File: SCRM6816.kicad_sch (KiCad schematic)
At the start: 10 parts, among them U1 68HC000P16, U24 74HC08, U6 74HC32, U7 74HC14, U8 74HC05, X1 CXO_DIP8_16MHz

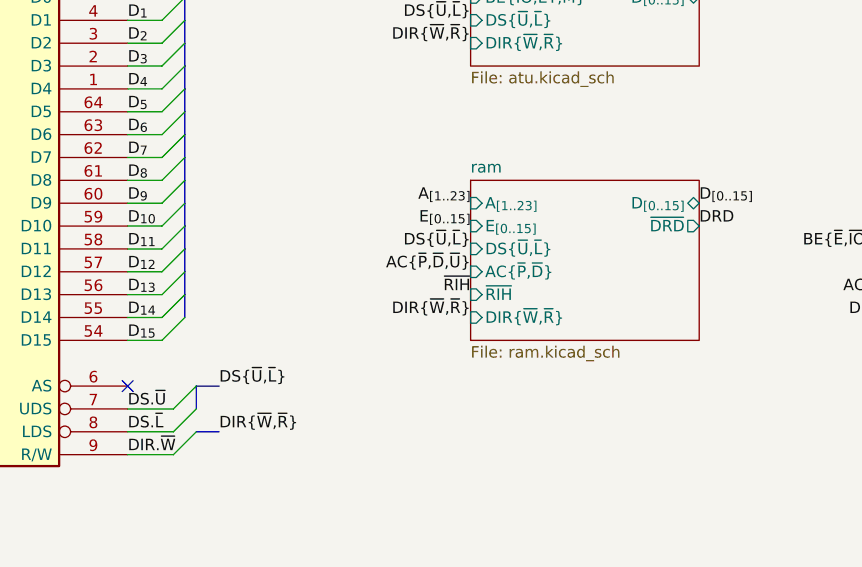
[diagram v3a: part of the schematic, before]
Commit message: apparently the ram was enabled all the time, ram.kicad_sch didn't even require BE.M... 	like whaaaaaaaa how did i let this happen oh my god sometimes im just braindead.
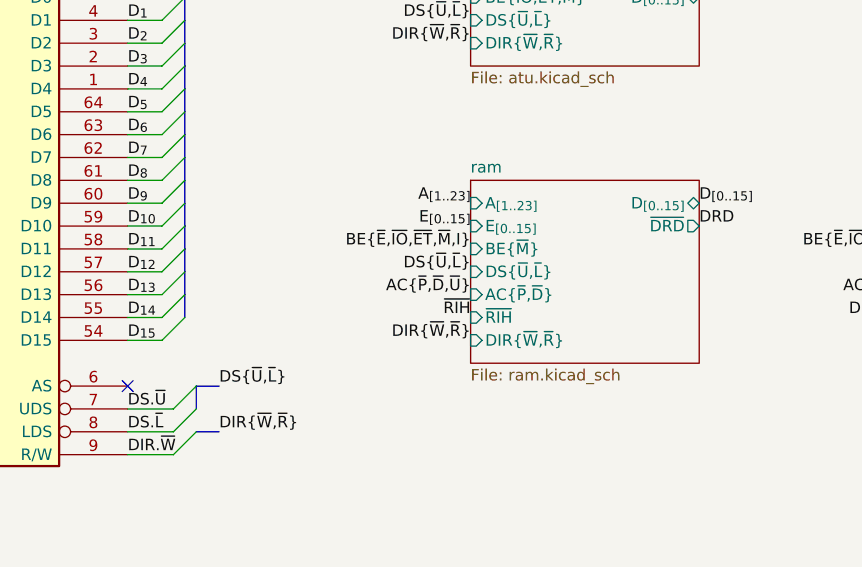
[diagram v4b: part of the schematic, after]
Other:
- sheet ram ports: added BE{~{M}}; removed none
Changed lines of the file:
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@@
 	)
 	(label "AC{~{P},~{D},~{U}}"
-		(at 127 124.46 180)
+		(at 127 127 180)
 		(effects
 			(font
@@
 	)
 	(label "DS{~{U},~{L}}"
-		(at 127 121.92 180)
+		(at 127 124.46 180)
 		(effects
 			(font
@@
 	)
 	(label "~{RIH}"
-		(at 127 127 180)
+		(at 127 129.54 180)
 		(effects
 			(font
@@
 	)
 	(label "DIR{~{W},~{R}}"
-		(at 127 129.54 180)
+		(at 127 132.08 180)
 		(effects
 			(font
@@
 		)
 	)
+	(label "BE{~{E},~{IO},~{ET},~{M},I}"
+		(at 127 121.92 180)
+		(effects
+			(font
+				(size 1.27 1.27)
+			)
+			(justify right bottom)
+		)
+	)
 	(label "~{I_{2}}"
 		(at 38.1 45.72 180)
@@
 	(sheet
 		(at 127 114.3)
-		(size 25.4 17.78)
+		(size 25.4 20.32)
 		(exclude_from_sim no)
 		(in_bom yes)
@@
 		)
 		(property "Sheetfile" "ram.kicad_sch"
-			(at 127 132.6646 0)
+			(at 127 135.2046 0)
 			(effects
 				(font
@@
 		)
 		(pin "AC{~{P},~{D}}" input
-			(at 127 124.46 180)
+			(at 127 127 180)
 			(effects
 				(font
@@
 		)
 		(pin "DIR{~{W},~{R}}" input
-			(at 127 129.54 180)
+			(at 127 132.08 180)
 			(effects
 				(font
@@
 		)
 		(pin "DS{~{U},~{L}}" input
-			(at 127 121.92 180)
+			(at 127 124.46 180)
 			(effects
 				(font
@@
 		)
 		(pin "~{RIH}" input
-			(at 127 127 180)
+			(at 127 129.54 180)
 			(effects
 				(font
@@
 			)
 		)
+		(pin "BE{~{M}}" input
+			(at 127 121.92 180)
+			(effects
+				(font
+					(size 1.27 1.27)
+				)
+				(justify left)
+			)
+		)

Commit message: [scheme] no major changes
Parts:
- added U28: 74HC74, symbol 74xx:74HC74
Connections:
- net +5V: now also U28.1 (~{R}), U28.10 (~{S}), U28.13 (~{R}), U28.4 (~{S})
- new net: U28.2 (D), U28.6 (~{Q})
- new net: U28.12 (D), U28.8 (~{Q})
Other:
- note added: "frequency dependent parts: - C1-R4 (rom's DRD timer) - C4-R12 (ilatch's timeout timer)"
- moved on the sheet: X1

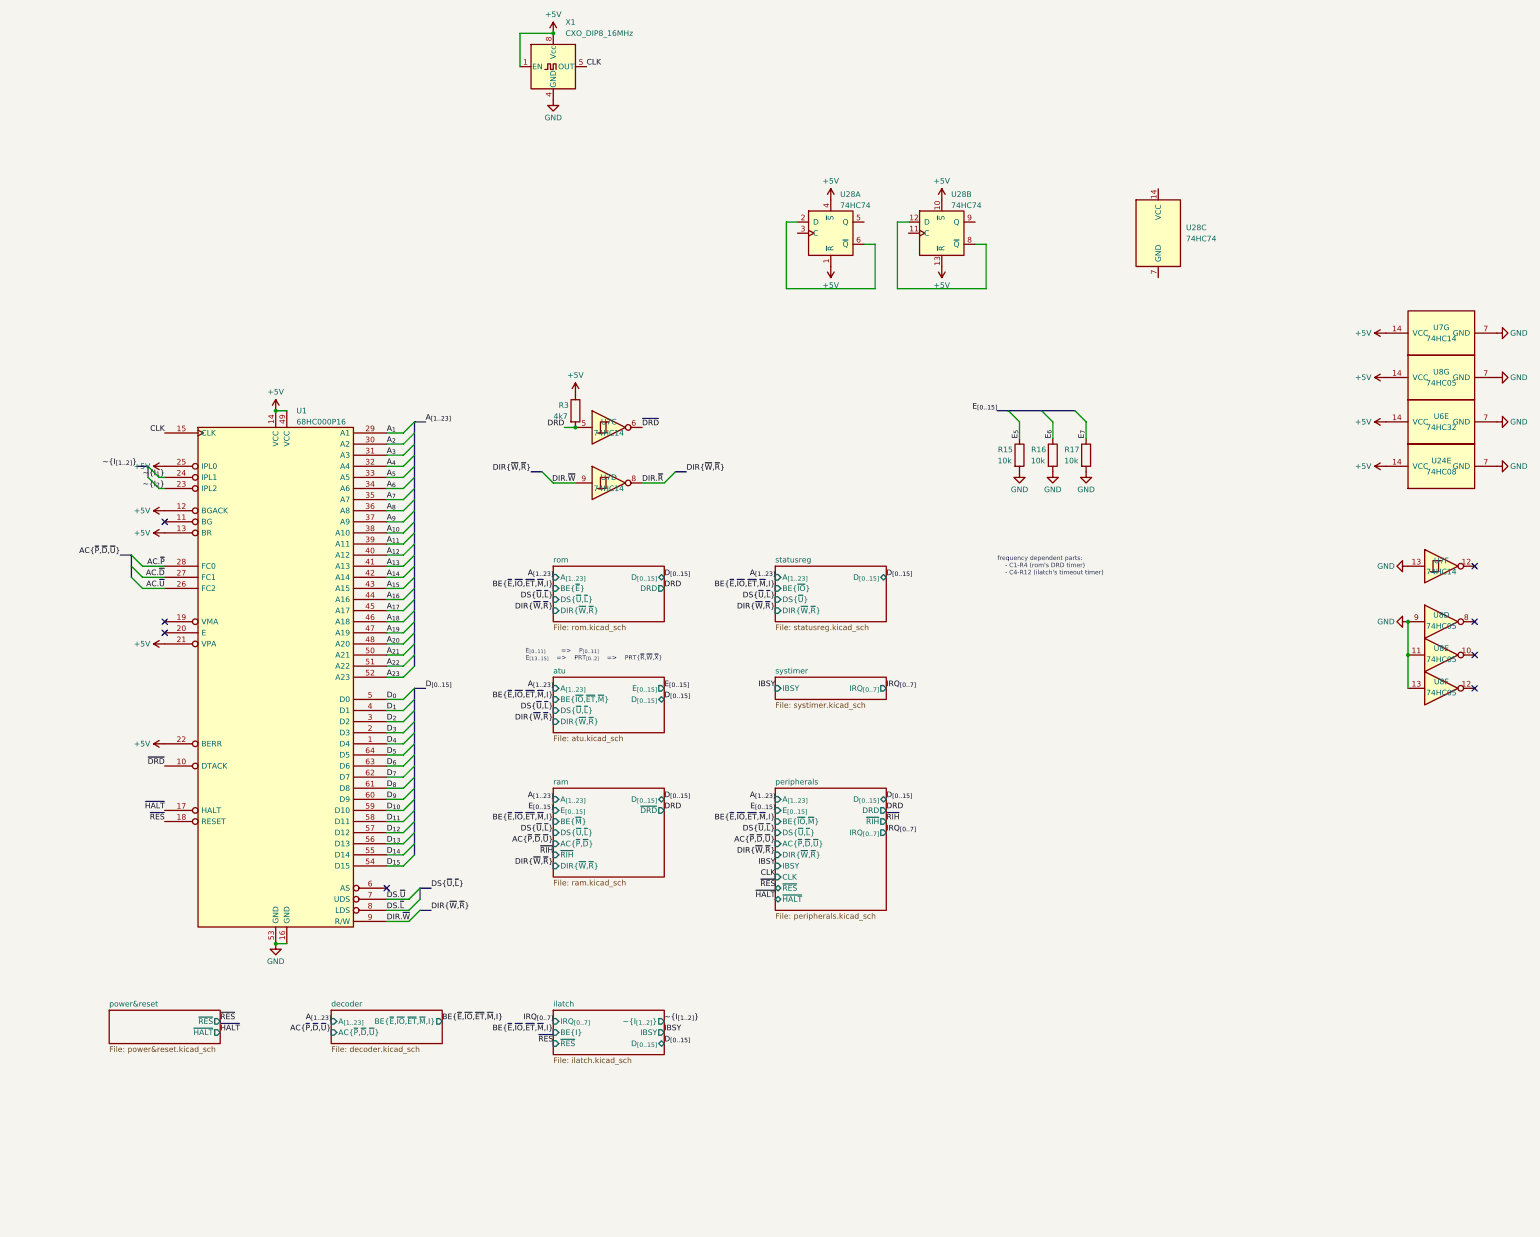
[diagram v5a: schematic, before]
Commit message: first commit: scheme ok [decoder]: 	- new spv. address space [mmu]: 	- removed pidreg 	- switched back to 8Kb mmu rams [ram/peripherals]: 	- added ground pins to connectors [misc]: 	- added DMA support 	- added clock halfer
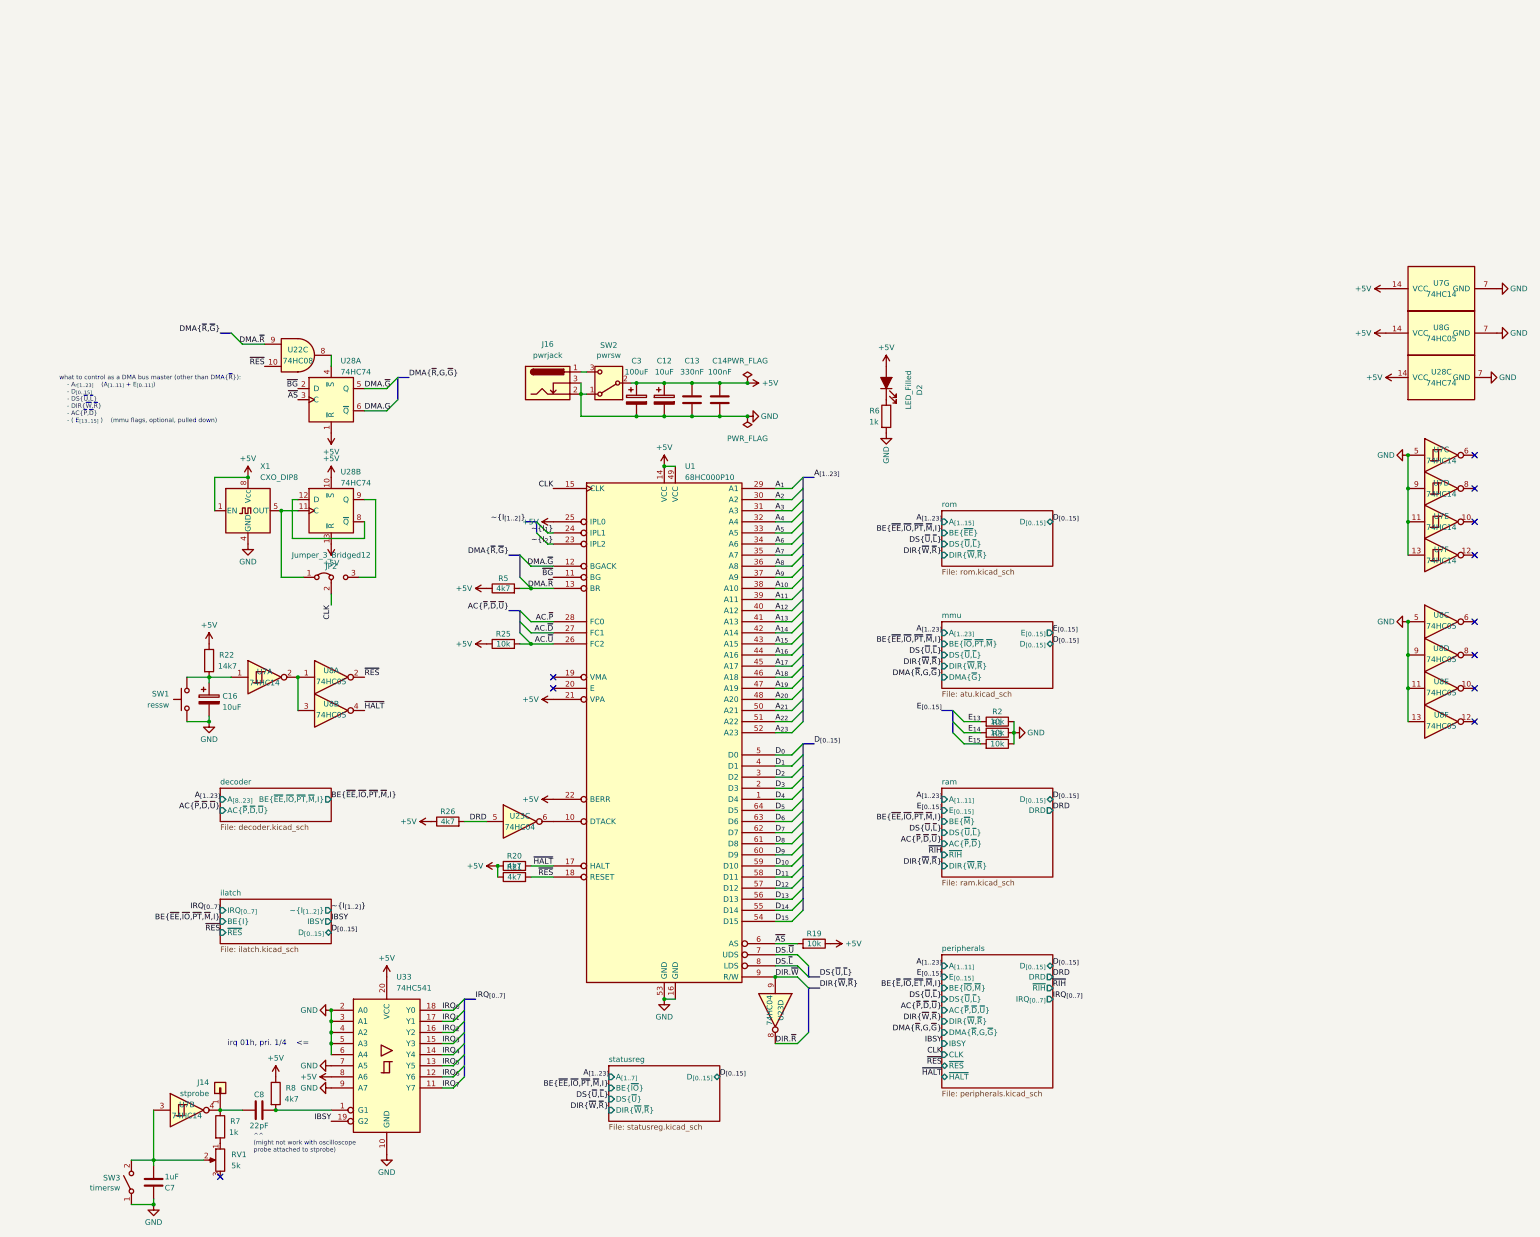
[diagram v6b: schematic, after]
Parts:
- removed R15, R16, R17: 10k, Resistor_THT:R_Axial_DIN0207_L6.3mm_D2.5mm_P2.54mm_Vertical, symbol Device:R
- removed U24: 74HC08, Package_DIP:DIP-14_W7.62mm, symbol 74xx:74LS08
- removed U6: 74HC32, Package_DIP:DIP-14_W7.62mm, symbol 74xx:74LS32
- added C12, C16: 10uF, Capacitor_THT:CP_Radial_D5.0mm_P2.00mm, symbol Device:C_Polarized
- added C13: 330nF, Capacitor_THT:C_Disc_D3.0mm_W1.6mm_P2.54mm, symbol Device:C
- added C14: 100nF, Capacitor_THT:C_Disc_D3.0mm_W1.6mm_P2.54mm, symbol Device:C
- added C3: 100uF, Capacitor_THT:CP_Radial_D8.0mm_P3.50mm, symbol Device:C_Polarized
- added C7: 1uF, Capacitor_THT:C_Disc_D3.0mm_W1.6mm_P2.54mm, symbol Device:C
- added C8: 22pF, Capacitor_THT:C_Disc_D3.0mm_W1.6mm_P2.54mm, symbol Device:C
- added D2: LED_Filled, LED_THT:LED_D5.0mm, symbol Device:LED_Filled
- added J14: stprobe, symbol Connector_Generic:Conn_01x01
- added J16: pwrjack, Connector_BarrelJack:BarrelJack_Horizontal, symbol Connector:Barrel_Jack_Switch
- added JP2: Jumper_3_Bridged12, symbol Jumper:Jumper_3_Bridged12
- added R1, R19, R2, R25: 10k, Resistor_THT:R_Axial_DIN0207_L6.3mm_D2.5mm_P2.54mm_Vertical, symbol Device:R
- added R20, R21, R26, R5, R8: 4k7, Resistor_THT:R_Axial_DIN0207_L6.3mm_D2.5mm_P2.54mm_Vertical, symbol Device:R
- added R22: 14k7, Resistor_THT:R_Axial_DIN0207_L6.3mm_D2.5mm_P2.54mm_Vertical, symbol Device:R
- added R6, R7: 1k, Resistor_THT:R_Axial_DIN0207_L6.3mm_D2.5mm_P2.54mm_Vertical, symbol Device:R
- added RV1: 5k, Potentiometer_THT:Potentiometer_Bourns_3386P_Vertical, symbol Device:R_Potentiometer
- added SW1: ressw, Connector_PinHeader_2.54mm:PinHeader_1x02_P2.54mm_Vertical, symbol Switch:SW_Push
- added SW2: pwrsw, Connector_PinHeader_2.54mm:PinHeader_1x03_P2.54mm_Vertical, symbol Switch:SW_SPDT
- added SW3: timersw, Button_Switch_THT:SW_DIP_SPSTx01_Slide_9.78x4.72mm_W7.62mm_P2.54mm, symbol Switch:SW_SPST
- added U22: 74HC08, symbol 74xx:74LS08
- added U23: 74HC04, symbol 74xx:74LS04
- added U33: 74HC541, Package_DIP:DIP-20_W7.62mm, symbol 74xx:74LS541
- added unit 5 of U7
- added unit 2 of U7
- added unit 1 of U7
- added unit 1 of U8
- added unit 2 of U8
- added unit 3 of U8
- R3: value 4k7 -> 10k
- U1: value 68HC000P16 -> 68HC000P10
- X1: value CXO_DIP8_16MHz -> CXO_DIP8
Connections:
- net +5V: now also U28.14 (VCC), C12.1, C13.2, C14.2, C3.1, D2.2 (A), R19.1, R20.1, R21.1, R22.1, R25.1, R26.1, R5.1, R8.1, SW2.2 (B), U33.20 (VCC), U33.8 (A6); no longer R3.1, U1.12 (BGACK), U1.13 (BR), U28.4 (~{S})
- net AC.~{U}: now also R25.2
- net CLK: now also JP2.2 (C); no longer X1.5 (OUT)
- net DIR.~{R}: now also U23.8; no longer U7.8
- net DIR.~{W}: now also U23.9; no longer U7.9
- net DRD: now also R26.2, U23.5; no longer R3.2, U7.5
- net GND: now also R3.1, U28.7 (GND), U7.5, U7.9, C12.2, C13.1, C14.1, C16.2, C3.2, C7.1, J16.2, J16.3, R1.1, R2.1, R6.2, SW1.1, SW2.1 (A), SW3.1 (A), U33.10 (GND), U33.2 (A0), U33.3 (A1), U33.4 (A2), U33.5 (A3), U33.6 (A4), U33.7 (A5), U33.9 (A7), U7.11, U8.5
- net IBSY: now also U33.19 (G2)
- net ~{HALT}: now also R20.2, U8.4
- net ~{RES}: now also R21.2, U22.10, U8.2
- net DMA.G: now reaches U28.6 (~{Q})
- net DMA.G: no longer U28.2 (D)
- net ~{AS}: now reaches U28.3 (C)
- net ~{AS}: now also U1.6 (AS), R19.2
- net DMA.~{G}: now reaches U28.5 (Q)
- net DMA.~{G}: now also U1.12 (BGACK)
- net at U28.11 (C): now also X1.5 (OUT), JP2.1 (A)
- net at U28.9 (Q): now also JP2.3 (B)
- net ~{BG}: now reaches U1.11 (BG)
- net ~{BG}: now also U28.2 (D)
- net ~{DRD}: no longer names the net of U1.10 (DTACK)
- net ~{DRD}: now also U23.6; no longer U7.6
- new net: C8.2, R8.2, U33.1 (G1)
- new net: U22.8, U28.4 (~{S})
- new net: J16.1, SW2.3 (C)
- new net: C16.1, R22.2, SW1.2, U7.1
- new net: U7.2, U8.1, U8.3
- new net: C7.2, RV1.2, SW3.2 (B), U7.3
- new net: C8.1, J14.1 (Pin_1), R7.1, U7.4
- new net: D2.1 (K), R6.1
- new net: R7.2, RV1.1
- new net DMA.~{R}: R5.2, U1.13 (BR), U22.9
- new net E_{13}: R2.2
- new net E_{14}: R1.2
- new net E_{15}: R3.2
- new net IRQ_{0}: U33.18 (Y0)
- new net IRQ_{1}: U33.17 (Y1)
- new net IRQ_{2}: U33.16 (Y2)
- new net IRQ_{3}: U33.15 (Y3)
- new net IRQ_{4}: U33.14 (Y4)
- new net IRQ_{5}: U33.13 (Y5)
- new net IRQ_{6}: U33.12 (Y6)
- new net IRQ_{7}: U33.11 (Y7)
- no-connect marks 8 -> 11
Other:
- sheet atu renamed mmu
- removed sheet power&reset
- removed sheet systimer
- sheet decoder ports: added A_{[8..23]}, BE{~{EE},~{IO},~{PT},~{M},I}; removed A_{[1..23]}, BE{~{E},~{IO},~{ET},~{M},I}
- sheet mmu ports: added BE{~{IO},~{PT},~{M}}, DMA{~{G}}; removed BE{~{IO},~{ET},~{M}}
- sheet peripherals ports: added A_{[1..11]}, DMA{~{R},G,~{G}}; removed A_{[1..23]}
- sheet ram ports: added A_{[1..11]}, DRD; removed A_{[1..23]}, ~{DRD}
- sheet rom ports: added A_{[1..15]}, BE{~{EE}}; removed A_{[1..23]}, BE{~{E}}, DRD
- sheet statusreg ports: added A_{[1..7]}; removed A_{[1..23]}
- note added: "^^ (might not work with oscilloscope probe attached to stprobe)"
- note added: "irq 01h, pri. 1/4 <="
- note added: "what to control as a DMA bus master (other than DMA{~{R}}): - A_{r[1..23]} (A_{[1..11]} + E_{[0..11]}) - D_{[0..15]} - DS{~{U},~{L}} - DIR{~{W},~{R}} - AC{~{P},~{D}} - ( E_{[13..15]} ) (mmu flags, optional, pulled down)"
- note removed: "E_{[0..11]} => P_{[0..11]} E_{[13..15]} => PRT_{[0..2]} => PRT{~{R},~{W},~{X}}"
- note removed: "frequency dependent parts: - C1-R4 (rom's DRD timer) - C4-R12 (ilatch's timeout timer)"
- moved on the sheet: U1, U28A, U28B, U28C, U7D, U7F, U7G, U8D, U8E, U8F, U8G, X1

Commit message: assigned footprints
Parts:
- J14: footprint (none) -> Connector_PinHeader_2.54mm:PinHeader_1x01_P2.54mm_Vertical
- JP2: footprint (none) -> Connector_PinHeader_2.54mm:PinHeader_1x03_P2.54mm_Vertical
- U22, U23, U28: footprint (none) -> Package_DIP:DIP-14_W7.62mm
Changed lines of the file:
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@@
 			)
 		)
-		(property "Footprint" ""
+		(property "Footprint" "Package_DIP:DIP-14_W7.62mm"
 			(at 330.2 20.32 0)
 			(effects
@@
 			)
 		)
-		(property "Footprint" ""
+		(property "Footprint" "Package_DIP:DIP-14_W7.62mm"
 			(at 119.38 121.92 0)
 			(effects
@@
 			)
 		)
-		(property "Footprint" ""
+		(property "Footprint" "Package_DIP:DIP-14_W7.62mm"
 			(at 76.2 25.4 0)
 			(effects
@@
 			)
 		)
-		(property "Footprint" ""
+		(property "Footprint" "Connector_PinHeader_2.54mm:PinHeader_1x03_P2.54mm_Vertical"
 			(at 76.2 66.04 0)
 			(effects
@@
 			)
 		)
-		(property "Footprint" ""
+		(property "Footprint" "Package_DIP:DIP-14_W7.62mm"
 			(at 177.8 165.1 0)
 			(effects
@@
 			)
 		)
-		(property "Footprint" ""
+		(property "Footprint" "Package_DIP:DIP-14_W7.62mm"
 			(at 76.2 50.8 0)
 			(effects
@@
 			)
 		)
-		(property "Footprint" ""
+		(property "Footprint" "Package_DIP:DIP-14_W7.62mm"
 			(at 68.58 15.24 0)
 			(effects
@@
 			)
 		)
-		(property "Footprint" ""
+		(property "Footprint" "Connector_PinHeader_2.54mm:PinHeader_1x01_P2.54mm_Vertical"
 			(at 50.8 182.88 0)
 			(effects
